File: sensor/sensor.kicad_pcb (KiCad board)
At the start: 2 copper layers, 57.1 x 76.2 mm, 9 parts, among them T1 DS18B20, T2 DS18B20, U1 DHT22, U9 SSCDRNN015PASA5

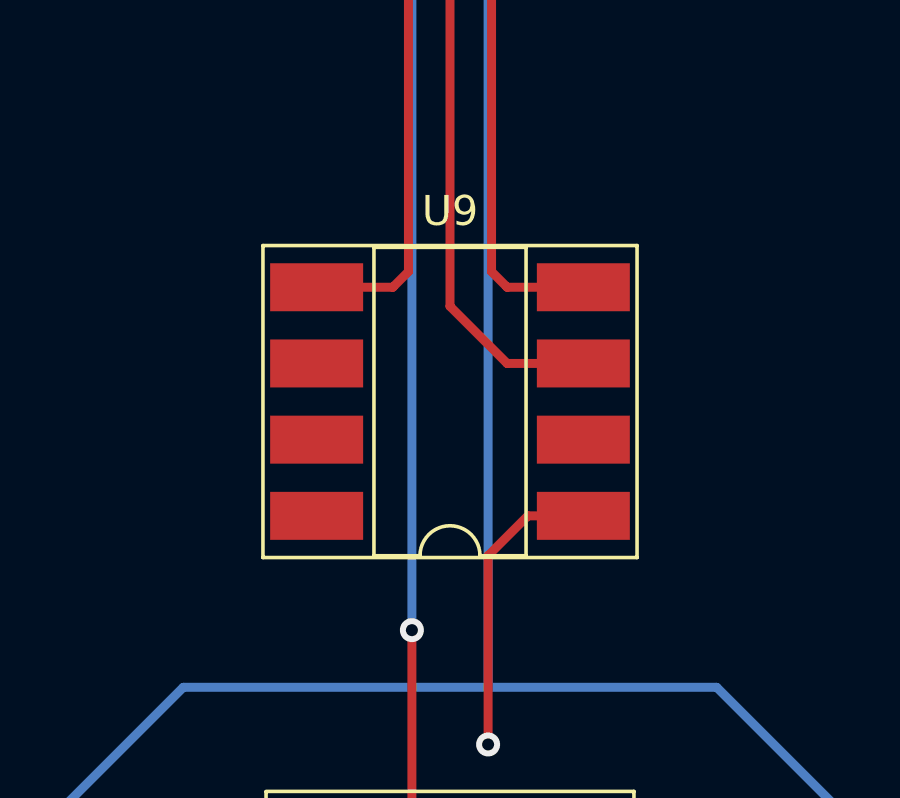
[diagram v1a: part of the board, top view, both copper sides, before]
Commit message: fix pressure sensor footprint
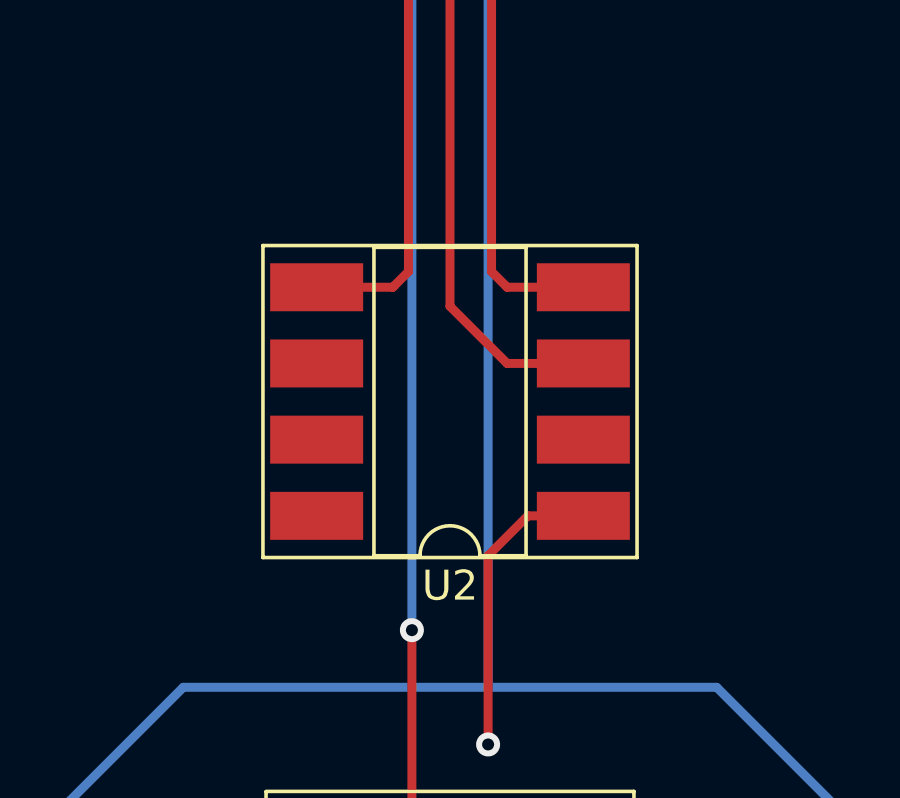
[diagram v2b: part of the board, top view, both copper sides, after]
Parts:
- removed U9: SSCDRNN015PASA5, Package_DIP:DIP-8_W8.89mm_SMDSocket_LongPads
- added U2: SSCDRNN015PASA5, Package_DIP:DIP-8_W8.89mm_SMDSocket_LongPads, F.Cu at (206.4, 94.6)
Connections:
- net SPI-SDA renamed SPI-MOSI
- DSUB2 pad 3: SPI-SDO -> SPI-MISO
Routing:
- net SPI-SDO: track 45.2 -> 0.00 mm
- net SPI-MISO: track 0.00 -> 45.2 mm

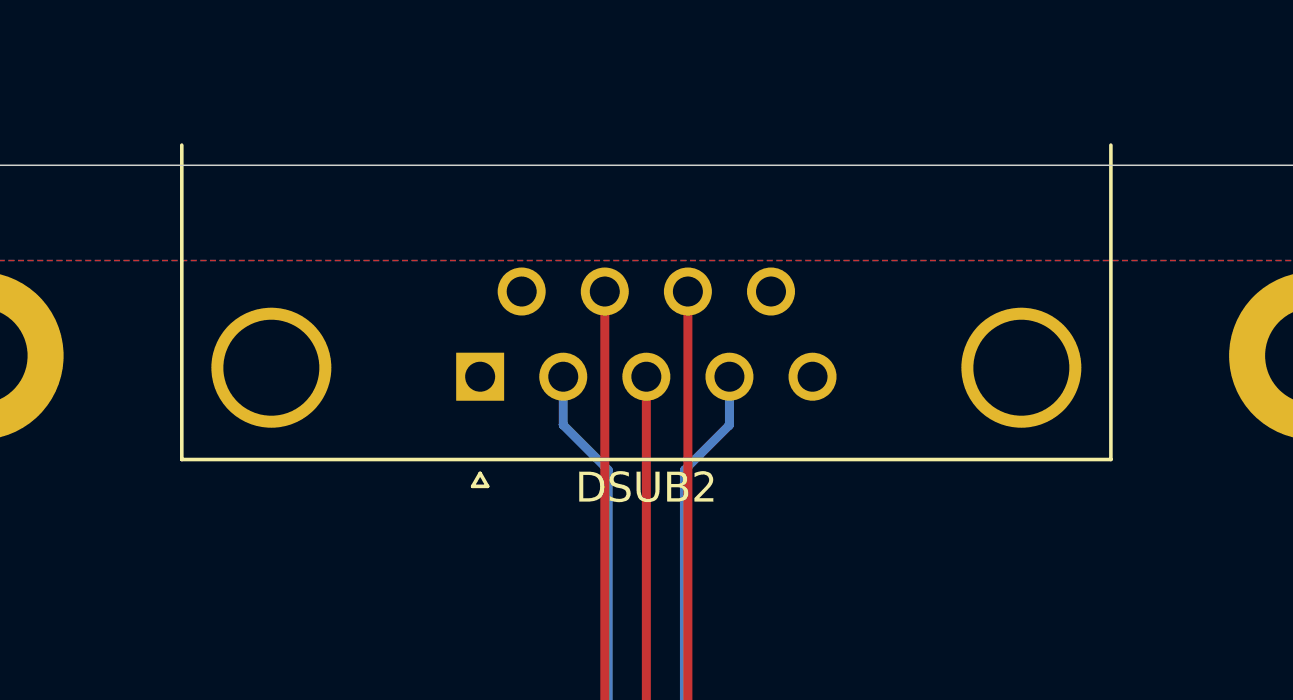
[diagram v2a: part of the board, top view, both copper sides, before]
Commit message: add db9 models, and update footprints
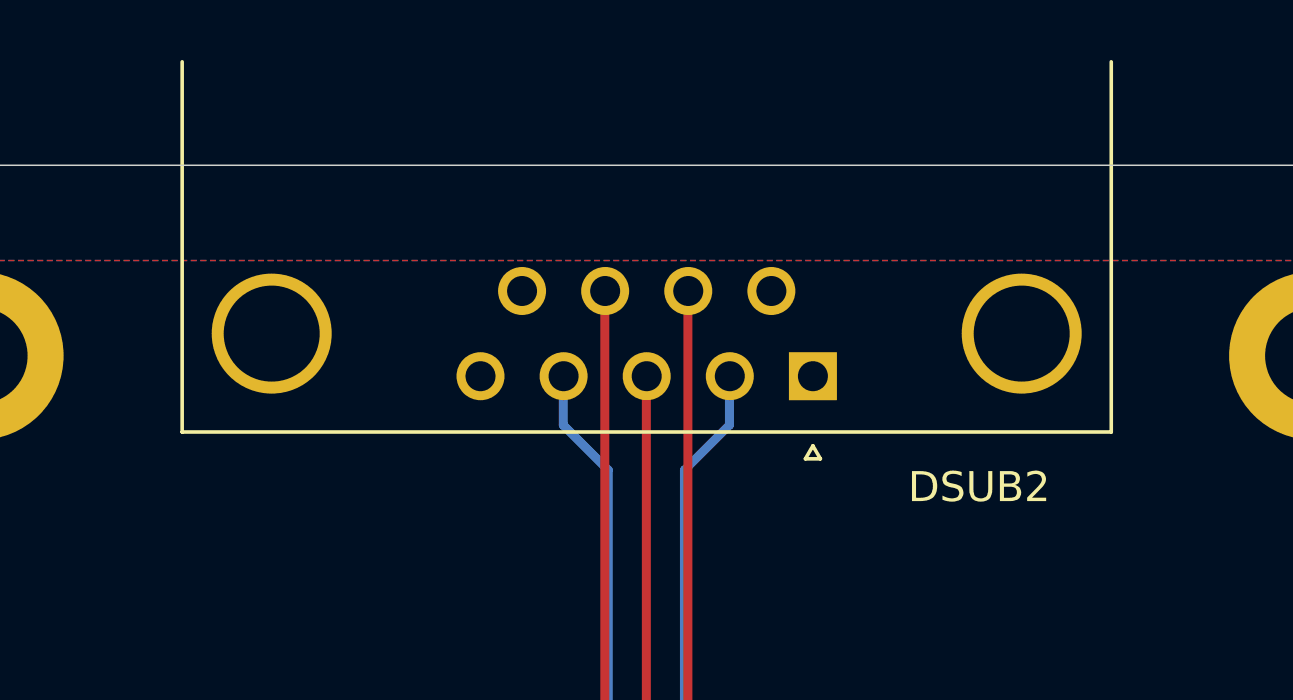
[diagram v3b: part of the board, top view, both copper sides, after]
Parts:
- DSUB2: value DB9_Female -> DB9_Male; footprint Connector_Dsub:DSUB-9_Female_Horizontal_P2.77x2.84mm_EdgePinOffset4.94mm_Housed_MountingHolesOffset7.48mm -> Connector_Dsub:DSUB-9_Male_Horizontal_P2.77x2.84mm_EdgePinOffset7.70mm_Housed_MountingHolesOffset9.12mm
- moved DSUB2 11.1 mm to (211.9, 51.5)
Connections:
- DSUB2 pad 1: GND -> +5V
- DSUB2 pad 2: DHT22 -> 1Wire
- DSUB2 pad 4: 1Wire -> DHT22
- DSUB2 pad 5: +5V -> GND
- DSUB2 pad 6: SPI-MOSI -> Net-(DSUB2-Pad6)
- DSUB2 pad 7: SPI-SS-Pressure -> SPI-CLK
- DSUB2 pad 8: SPI-CLK -> SPI-SS-Pressure
- DSUB2 pad 9: Net-(DSUB2-Pad9) -> SPI-MOSI

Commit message: WIP sensor PCB
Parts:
- removed DSUB2: DB9_Male, Connector_Dsub:DSUB-9_Male_Horizontal_P2.77x2.84mm_EdgePinOffset7.70mm_Housed_MountingHolesOffset9.12mm
- removed the REF** at (228.6, 114.3)
- removed the REF** at (184.2, 114.3)
- removed the REF** at (184.2, 50.8)
- removed the REF** at (228.6, 50.8)
- removed T1, T2: DS18B20, Package_TO_SOT_THT:TO-92_Inline_Wide
- added D1: LED, LED_SMD:LED_0805_2012Metric_Pad1.15x1.40mm_HandSolder, F.Cu at (142.9, 70.5)
- added D10: LED, LED_SMD:LED_0805_2012Metric_Pad1.15x1.40mm_HandSolder, F.Cu at (142.9, 78.1)
- added D11: LED, LED_SMD:LED_0805_2012Metric_Pad1.15x1.40mm_HandSolder, F.Cu at (142.9, 83.2)
- added D12: LED, LED_SMD:LED_0805_2012Metric_Pad1.15x1.40mm_HandSolder, F.Cu at (142.9, 88.3)
- added D13: LED, LED_SMD:LED_0805_2012Metric_Pad1.15x1.40mm_HandSolder, F.Cu at (173.2, 86.0)
- added D14: LED, LED_SMD:LED_0805_2012Metric_Pad1.15x1.40mm_HandSolder, F.Cu at (173.2, 80.9)
- added D15: LED, LED_SMD:LED_0805_2012Metric_Pad1.15x1.40mm_HandSolder, F.Cu at (173.2, 75.8)
- added D16: LED, LED_SMD:LED_0805_2012Metric_Pad1.15x1.40mm_HandSolder, F.Cu at (173.2, 70.7)
- added D2: LED, LED_SMD:LED_0805_2012Metric_Pad1.15x1.40mm_HandSolder, F.Cu at (142.9, 75.6)
- added D3: LED, LED_SMD:LED_0805_2012Metric_Pad1.15x1.40mm_HandSolder, F.Cu at (142.9, 80.6)
- added D4: LED, LED_SMD:LED_0805_2012Metric_Pad1.15x1.40mm_HandSolder, F.Cu at (142.9, 85.7)
- added D5: LED, LED_SMD:LED_0805_2012Metric_Pad1.15x1.40mm_HandSolder, F.Cu at (173.2, 88.5)
- added D6: LED, LED_SMD:LED_0805_2012Metric_Pad1.15x1.40mm_HandSolder, F.Cu at (173.2, 83.4)
- added D7: LED, LED_SMD:LED_0805_2012Metric_Pad1.15x1.40mm_HandSolder, F.Cu at (173.2, 78.3)
- added D8: LED, LED_SMD:LED_0805_2012Metric_Pad1.15x1.40mm_HandSolder, F.Cu at (173.2, 73.3)
- added D9: LED, LED_SMD:LED_0805_2012Metric_Pad1.15x1.40mm_HandSolder, F.Cu at (142.9, 73.0)
- added J1: Conn_01x08_Female, Stardust:691382040008, F.Cu at (157.4, 60.9)
- added R1: R10k, Resistor_SMD:R_0603_1608Metric_Pad0.98x0.95mm_HandSolder, F.Cu at (153.9, 70.6)
- added R10: R330, Resistor_SMD:R_0603_1608Metric, F.Cu at (166.8, 88.5)
- added R11: R330, Resistor_SMD:R_0603_1608Metric, F.Cu at (166.8, 86.0)
- added R12: R330, Resistor_SMD:R_0603_1608Metric, F.Cu at (166.8, 83.4)
- added R13: R330, Resistor_SMD:R_0603_1608Metric, F.Cu at (166.8, 80.9)
- added R14: R330, Resistor_SMD:R_0603_1608Metric, F.Cu at (166.8, 78.3)
- added R15: R330, Resistor_SMD:R_0603_1608Metric, F.Cu at (166.8, 75.8)
- added R16: R330, Resistor_SMD:R_0603_1608Metric, F.Cu at (166.8, 73.3)
- added R17: R330, Resistor_SMD:R_0603_1608Metric, F.Cu at (166.8, 70.7)
- added R2: R330, Resistor_SMD:R_0603_1608Metric, F.Cu at (147.9, 70.5)
- added R3: R330, Resistor_SMD:R_0603_1608Metric, F.Cu at (147.9, 73.0)
- added R4: R330, Resistor_SMD:R_0603_1608Metric, F.Cu at (147.9, 75.6)
- added R5: R330, Resistor_SMD:R_0603_1608Metric, F.Cu at (147.9, 78.1)
- added R6: R330, Resistor_SMD:R_0603_1608Metric, F.Cu at (147.9, 80.6)
- added R7: R330, Resistor_SMD:R_0603_1608Metric, F.Cu at (147.9, 83.2)
- added R8: R330, Resistor_SMD:R_0603_1608Metric, F.Cu at (147.9, 85.7)
- added R9: R330, Resistor_SMD:R_0603_1608Metric, F.Cu at (147.9, 88.3)
- added REF**: LED_D3.0mm, LED_THT:LED_D3.0mm, F.Cu at (178.2, 76.6)
- added REF**: MountingHole_2.5mm_Pad, MountingHole:MountingHole_2.5mm_Pad, F.Cu at (136.1, 119.8)
- added REF**: MountingHole_2.5mm_Pad, MountingHole:MountingHole_2.5mm_Pad, F.Cu at (178.8, 119.8)
- added REF**: MountingHole_2.5mm_Pad, MountingHole:MountingHole_2.5mm_Pad, F.Cu at (178.8, 60.4)
- added REF**: MountingHole_2.5mm_Pad, MountingHole:MountingHole_2.5mm_Pad, F.Cu at (136.1, 60.4)
- added U3: TCA9555DBR, Package_SO:SSOP-24_5.3x8.2mm_P0.65mm, F.Cu at (157.4, 78.9)
- U1: footprint Sensor:Aosong_DHT11_5.5x12.0_P2.54mm -> Stardust:DHT22_15.0x25.0_P2.54mm_Horizontal
- moved U2 59.6 mm to (147.8, 105.9)
- moved U1 35.7 mm to (170.0, 95.8), turned to 270 degrees
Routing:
- net 1Wire: track 87.4 -> 0.00 mm
- net DHT22: track 59.6 -> 36.5 mm, vias 1 -> 0
- net SDA: track 0.00 -> 17.3 mm
- net SCL: track 0.00 -> 17.3 mm
- net Net-(R2-Pad2): track 0.00 -> 10.9 mm
- net Net-(R17-Pad2): track 0.00 -> 10.4 mm
- net Net-(R9-Pad2): track 0.00 -> 10.0 mm
- net Net-(R10-Pad2): track 0.00 -> 9.04 mm
- net Net-(R3-Pad2): track 0.00 -> 8.97 mm
- net +5V: track 0.00 -> 8.94 mm, vias 0 -> 3
- net Net-(R16-Pad2): track 0.00 -> 8.46 mm
- net Net-(R8-Pad2): track 0.00 -> 8.14 mm
- net Net-(R11-Pad2): track 0.00 -> 7.81 mm
- net Net-(R4-Pad2): track 0.00 -> 6.70 mm
- net Net-(R15-Pad2): track 0.00 -> 6.56 mm
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- added copper zone on B.Cu, net +5V
- added copper zone on F.Cu, net GND
- removed copper zone on F.Cu, net +5V
- removed copper zone on B.Cu, net GND
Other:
- board size 57.1 x 76.2 mm -> 51.7 x 68.4 mm
- board text added: "Stardust 2021"
- board text added: "hi@y4s.io"
- board text removed: "2020"
- board text removed: "Stardust"
- board text removed: "contact@yasiu.pl"

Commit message: WIP sensor PCB - delete files
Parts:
- removed the REF** at (178.2, 76.6)

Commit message: WIP
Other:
- board text added: "SimLE Stardust 2021"
- board text removed: "Stardust 2021"

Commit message: change everything
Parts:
- removed D13, D14, D15, D16, D5, D6, D7, D8: LED, LED_SMD:LED_0805_2012Metric_Pad1.15x1.40mm_HandSolder
- removed R10, R11, R12, R13, R14, R15, R16, R17: R330, Resistor_SMD:R_0603_1608Metric
- removed REF** (x4): MountingHole_2.5mm_Pad, MountingHole:MountingHole_2.5mm_Pad
- added A0-H1: 0R, Resistor_SMD:R_0603_1608Metric_Pad0.98x0.95mm_HandSolder, F.Cu at (163.3, 76.1)
- added A0-L1: 0R, Resistor_SMD:R_0603_1608Metric_Pad0.98x0.95mm_HandSolder, F.Cu at (164.8, 76.1)
- added A1-H1: 0R, Resistor_SMD:R_0603_1608Metric_Pad0.98x0.95mm_HandSolder, F.Cu at (150.8, 74.0)
- added A1-L1: 0R, Resistor_SMD:R_0603_1608Metric_Pad0.98x0.95mm_HandSolder, F.Cu at (149.3, 74.0)
- D1, D10, D11, D12, D2, D3, D4, D9: footprint LED_SMD:LED_0805_2012Metric_Pad1.15x1.40mm_HandSolder -> LED_THT:LED_D5.0mm
- moved D12 38.4 mm to (174.8, 67.0), turned to 180 degrees
- moved D4 34.0 mm to (174.8, 74.0), turned to 180 degrees
- moved D3 32.8 mm to (174.8, 88.0), turned to 180 degrees
- moved D11 32.0 mm to (174.8, 81.0), turned to 180 degrees
- moved R9 28.7 mm to (168.8, 68.5), turned to 270 degrees
- moved R8 23.2 mm to (168.8, 75.5), turned to 270 degrees
- moved R6 21.6 mm to (168.8, 86.0), turned to 90 degrees
- moved R7 21.2 mm to (168.8, 79.5), turned to 90 degrees
- moved D10 10.4 mm to (139.8, 88.0)
- moved R5 8.70 mm to (145.8, 86.5), turned to 90 degrees
- moved D2 6.26 mm to (139.8, 81.0)
- moved R4 4.66 mm to (145.8, 79.7), turned to 90 degrees
- moved D1 4.59 mm to (139.8, 67.0)
- moved R3 3.54 mm to (145.8, 75.9), turned to 270 degrees
- moved D9 3.20 mm to (139.8, 74.0)
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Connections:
- U1 pad 3: Net-(U1-Pad3) -> (no net)
- U3 pad 10: Net-(R8-Pad2) -> (no net)
- U3 pad 11: Net-(R9-Pad2) -> (no net)
- U3 pad 13: Net-(R10-Pad2) -> Net-(R6-Pad2)
- U3 pad 14: Net-(R11-Pad2) -> Net-(R7-Pad2)
- U3 pad 15: Net-(R12-Pad2) -> Net-(R8-Pad2)
- U3 pad 16: Net-(R13-Pad2) -> Net-(R9-Pad2)
- U3 pad 17: Net-(R14-Pad2) -> (no net)
- U3 pad 18: Net-(R15-Pad2) -> (no net)
- U3 pad 19: Net-(R16-Pad2) -> (no net)
- U3 pad 2: GND -> Net-(A1-H1-Pad2)
- U3 pad 20: Net-(R17-Pad2) -> (no net)
- U3 pad 21: GND -> Net-(A0-H1-Pad2)
- U3 pad 8: Net-(R6-Pad2) -> (no net)
- U3 pad 9: Net-(R7-Pad2) -> (no net)
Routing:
- net Net-(R17-Pad2): track 10.4 -> 0.00 mm
- net Net-(R10-Pad2): track 9.04 -> 0.00 mm
- net Net-(R16-Pad2): track 8.46 -> 0.00 mm
- net Net-(R11-Pad2): track 7.81 -> 0.00 mm
- net Net-(R9-Pad2): track 10.0 -> 17.6 mm
- net Net-(R5-Pad2): track 5.54 -> 12.6 mm
- net Net-(R15-Pad2): track 6.56 -> 0.00 mm
- net Net-(R12-Pad2): track 5.91 -> 0.00 mm
- net Net-(R14-Pad2): track 5.61 -> 0.00 mm
- net +5V: track 8.94 -> 14.3 mm, vias 3 -> 4
- net Net-(R13-Pad2): track 5.12 -> 0.00 mm
- net Net-(A1-H1-Pad2): track 0.00 -> 4.98 mm
- net Net-(D8-Pad2): track 4.50 -> 0.00 mm
- net Net-(D7-Pad2): track 4.50 -> 0.00 mm
- net Net-(D6-Pad2): track 4.50 -> 0.00 mm
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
